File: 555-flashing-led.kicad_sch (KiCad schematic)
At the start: 6 parts, among them U1 7555

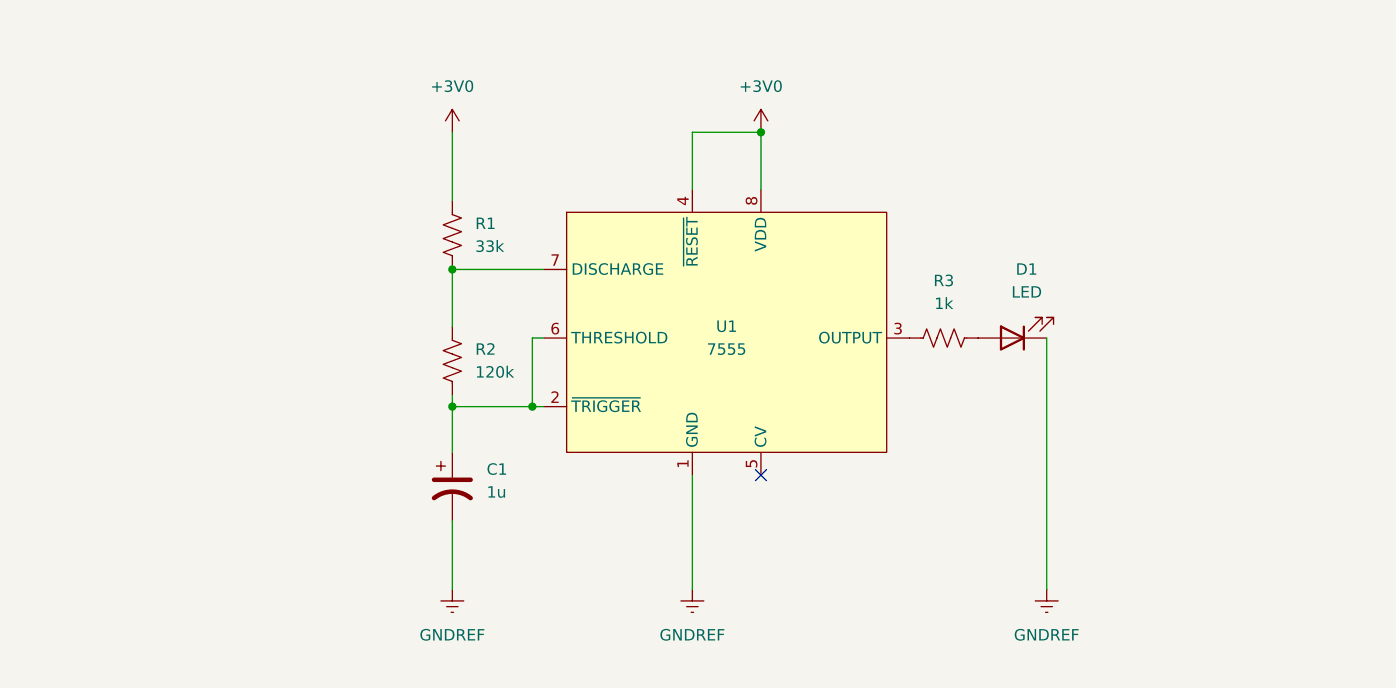
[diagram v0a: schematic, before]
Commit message: arrange PCB component (#1)
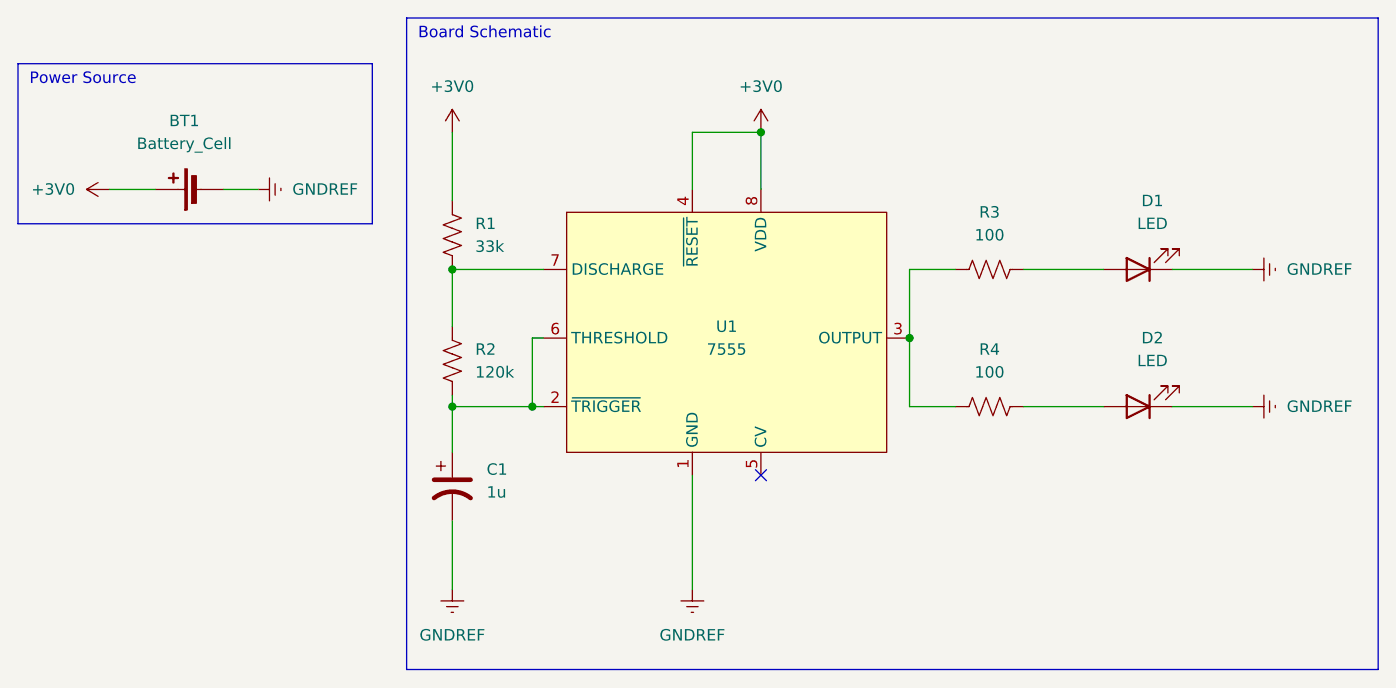
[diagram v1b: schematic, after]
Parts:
- added BT1: Battery_Cell, Battery:BatteryHolder_Keystone_107_1x23mm, symbol Device:Battery_Cell
- added D2: LED, LED_THT:LED_D5.0mm, symbol Device:LED
- added R4: 100, Resistor_THT:R_Axial_DIN0309_L9.0mm_D3.2mm_P15.24mm_Horizontal, symbol Device:R_US
- C1: footprint (none) -> Capacitor_THT:CP_Radial_D5.0mm_P2.50mm
- D1: footprint (none) -> LED_THT:LED_D5.0mm
- R1, R2: footprint (none) -> Resistor_THT:R_Axial_DIN0309_L9.0mm_D3.2mm_P15.24mm_Horizontal
- R3: value 1k -> 100; footprint (none) -> Resistor_THT:R_Axial_DIN0309_L9.0mm_D3.2mm_P15.24mm_Horizontal
- U1: footprint (none) -> Package_DIP:DIP-8_W7.62mm_LongPads
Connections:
- net +3V0: now also BT1.1 (+)
- net GNDREF: now also BT1.2 (-), D2.1 (K)
- net at R3.1, U1.3 (OUTPUT): now also R4.1
- new net: D2.2 (A), R4.2
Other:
- note added: "Board Schematic"
- note added: "Power Source"
- moved on the sheet: D1, R3
